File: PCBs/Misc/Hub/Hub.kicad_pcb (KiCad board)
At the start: 2 copper layers, 175.3 x 29.2 mm, 25 parts, among them J1 Conn_02x04_Top_Bottom, J2 Conn_02x04_Top_Bottom, U2 RJ45-B-1*4, U3 RJ45-B-1*4

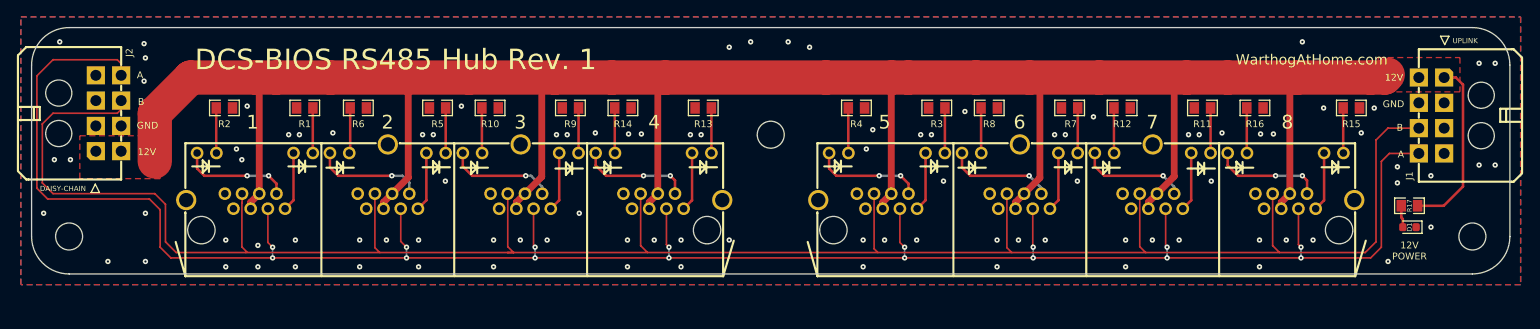
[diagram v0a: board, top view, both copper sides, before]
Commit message: Updated micro-fit pinout for more power
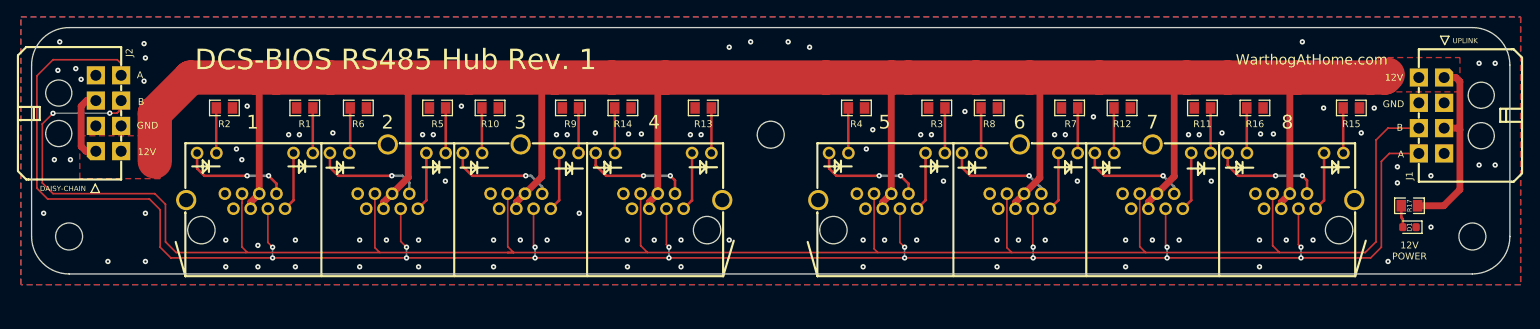
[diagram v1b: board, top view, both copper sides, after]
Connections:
- J1 pad 3: unconnected-(J1-Pad3) -> +12V
- J1 pad 4: unconnected-(J1-Pad4) -> GND
- J2 pad 3: unconnected-(J2-Pad3) -> +12V
- J2 pad 4: unconnected-(J2-Pad4) -> GND
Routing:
- net +12V: track 312.5 -> 323.0 mm
- net RS485-: track 259.2 -> 260.2 mm, vias 0 -> 2
- net GND: vias 98 -> 101

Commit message: Tweaked Hub
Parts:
- removed R1, R10, R11, R12, R13, R14, R15, R16, R2, R3, R4, R5, R6, R7, R8, R9: 1.8K, A10 KiCad Libraries:R0805
- added G***: LOGO, LOGO, F.Cu at (128.0, 85.2)
- added G***: LOGO, LOGO, F.Cu at (115.5, 89.2)
- added G***: LOGO, LOGO, B.Cu at (145.5, 100.5)
- added REF**: Tooling Hole, A10 KiCad Libraries:Tooling Hole, F.Cu at (216.8, 83.2)
- added REF**: Tooling Hole, A10 KiCad Libraries:Tooling Hole, F.Cu at (66.0, 110.0)
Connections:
- U2 pad 1: TX_LED1 -> GND
- U2 pad 10: TX_LED1 -> unconnected-(U2-Pad10)
- U2 pad 11: Net-(R2-Pad2) -> unconnected-(U2-Pad11)
- U2 pad 12: RX_LED1 -> unconnected-(U2-Pad12)
- U2 pad 13: TX_LED2 -> GND
- U2 pad 14: RX_LED2 -> +12V
- U2 pad 2: RX_LED1 -> +12V
- U2 pad 21: Net-(R5-Pad2) -> unconnected-(U2-Pad21)
- U2 pad 22: TX_LED2 -> unconnected-(U2-Pad22)
- U2 pad 23: Net-(R6-Pad2) -> unconnected-(U2-Pad23)
- U2 pad 24: RX_LED2 -> unconnected-(U2-Pad24)
- U2 pad 25: TX_LED3 -> GND
- U2 pad 26: RX_LED3 -> +12V
- U2 pad 33: Net-(R9-Pad2) -> unconnected-(U2-Pad33)
- U2 pad 34: TX_LED3 -> unconnected-(U2-Pad34)
- U2 pad 35: Net-(R10-Pad2) -> unconnected-(U2-Pad35)
- U2 pad 36: RX_LED3 -> unconnected-(U2-Pad36)
- U2 pad 37: TX_LED4 -> GND
- U2 pad 38: RX_LED4 -> +12V
- U2 pad 45: Net-(R13-Pad2) -> unconnected-(U2-Pad45)
- U2 pad 46: TX_LED4 -> unconnected-(U2-Pad46)
- U2 pad 47: Net-(R14-Pad2) -> unconnected-(U2-Pad47)
- U2 pad 48: RX_LED4 -> unconnected-(U2-Pad48)
- U2 pad 9: Net-(R1-Pad2) -> unconnected-(U2-Pad9)
- U3 pad 1: TX_LED5 -> GND
- U3 pad 10: TX_LED5 -> unconnected-(U3-Pad10)
- U3 pad 11: Net-(R4-Pad2) -> unconnected-(U3-Pad11)
- U3 pad 12: RX_LED5 -> unconnected-(U3-Pad12)
- U3 pad 13: TX_LED6 -> GND
- U3 pad 14: RX_LED6 -> +12V
- U3 pad 2: RX_LED5 -> +12V
- U3 pad 21: Net-(R7-Pad2) -> unconnected-(U3-Pad21)
- U3 pad 22: TX_LED6 -> unconnected-(U3-Pad22)
- U3 pad 23: Net-(R8-Pad2) -> unconnected-(U3-Pad23)
- U3 pad 24: RX_LED6 -> unconnected-(U3-Pad24)
- U3 pad 25: TX_LED7 -> GND
- U3 pad 26: RX_LED7 -> +12V
- U3 pad 33: Net-(R11-Pad2) -> unconnected-(U3-Pad33)
- U3 pad 34: TX_LED7 -> unconnected-(U3-Pad34)
- U3 pad 35: Net-(R12-Pad2) -> unconnected-(U3-Pad35)
- U3 pad 36: RX_LED7 -> unconnected-(U3-Pad36)
- U3 pad 37: TX_LED8 -> GND
- U3 pad 38: RX_LED8 -> +12V
- U3 pad 45: Net-(R15-Pad2) -> unconnected-(U3-Pad45)
- U3 pad 46: TX_LED8 -> unconnected-(U3-Pad46)
- U3 pad 47: Net-(R16-Pad2) -> unconnected-(U3-Pad47)
- U3 pad 48: RX_LED8 -> unconnected-(U3-Pad48)
- U3 pad 9: Net-(R3-Pad2) -> unconnected-(U3-Pad9)
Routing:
- net +12V: track 323.0 -> 489.3 mm
- net RX_LED1: track 13.2 -> 0.00 mm, vias 2 -> 0
- net RX_LED5: track 13.2 -> 0.00 mm, vias 2 -> 0
- net RX_LED4: track 13.2 -> 0.00 mm, vias 2 -> 0
- net RX_LED2: track 13.2 -> 0.00 mm, vias 1 -> 0
- net RX_LED8: track 13.2 -> 0.00 mm, vias 2 -> 0
- net RX_LED6: track 12.8 -> 0.00 mm, vias 1 -> 0
- net RX_LED7: track 12.8 -> 0.00 mm, vias 1 -> 0
- net RX_LED3: track 12.8 -> 0.00 mm, vias 1 -> 0
- net TX_LED7: track 7.02 -> 0.00 mm
- net TX_LED3: track 7.02 -> 0.00 mm
- net TX_LED8: track 7.01 -> 0.00 mm
- net TX_LED6: track 7.01 -> 0.00 mm
- net TX_LED5: track 7.01 -> 0.00 mm
- net TX_LED4: track 7.01 -> 0.00 mm
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- added copper zone on B.Cu, net +12V
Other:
- board text added: "${TITLE}"
- board text added: "2 12V"
- board text added: "DCSBIOSKit.com"
- board text added: "GND 1"
- board text added: "R. ${REVISION}"
- board text added: "WARNING! DO NOT CONNECT TO HOME NETWORK!"
- board text added: "WARNING! DO NOT HOTPLUG!"
- board text removed: "2 RX LED"
- board text removed: "BRRRRRRRRRRT"
- board text removed: "DCS-BIOS RS485 Hub Rev. 1"
- board text removed: "TX LED 1"
- board text removed: "WarthogAtHome.com"

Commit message: Updated HUB
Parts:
- removed the G*** at (115.5, 89.2)
- removed HOLE-2: MountingHole_3.2mm_M3, MountingHole:MountingHole_3.2mm_M3
- removed U2, U3: RJ45-B-1*4, A10 KiCad Libraries:RJ45-TH_B-1-4
- added HOLE-3: MountingHole_3.2mm_M3, MountingHole:MountingHole_3.2mm_M3, F.Cu at (70.0, 85.2)
- added HOLE-4: MountingHole_3.2mm_M3, MountingHole:MountingHole_3.2mm_M3, F.Cu at (219.2, 85.2)
- added RJ1: DS1130-S80BP, A10 KiCad Libraries:RJ45-TH_DS1130-S80BP, F.Cu at (144.5, 102.1)
- R1: renamed from R17; footprint A10 KiCad Libraries:R0805 -> Resistor_SMD:R_0603_1608Metric
- moved J1 13.2 mm to (213.2, 96.8)
- moved J2 11.0 mm to (75.9, 96.8)
- moved R1 10.9 mm to (211.0, 105.7)
- moved G*** 10.9 mm to (117.2, 86.5)
- moved D1 10.8 mm to (211.0, 107.3)
- moved HOLE-4 9.92 mm to (219.2, 108.2)
- moved REF** 8.00 mm to (74.0, 110.0)
- moved HOLE-3 7.42 mm to (70.0, 108.2)
- moved REF** 2.35 mm to (214.4, 83.2)
- moved G*** 0.58 mm to (144.9, 100.5)
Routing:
- net +12V: track 489.3 -> 371.6 mm
- net RS485-: track 260.7 -> 294.4 mm
- net RS485+: track 254.9 -> 284.0 mm
- net Net-(D1-Pad2): track 2.61 -> 1.56 mm
- net GND: vias 39 -> 89
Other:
- board size 175.3 x 29.2 mm -> 155.4 x 29.2 mm
- board text added: "POWER"
- board text added: "WARNING! DO NOT CONNECT TO HOME NETWORK! DO NOT HOTPLUG!"
- board text removed: "1"
- board text removed: "12V 5"
- board text removed: "12V POWER"
- board text removed: "2"
- board text removed: "2 12V"
- board text removed: "3"
- board text removed: "4"
- board text removed: "5"
- board text removed: "5 12V"
- board text removed: "6"
- board text removed: "6 B"
- board text removed: "7"
- board text removed: "8"
- board text removed: "8 GND"
- board text removed: "A 3"
- board text removed: "GND 1"
- board text removed: "GND 7"
- board text removed: "WARNING! DO NOT CONNECT TO HOME NETWORK!"
- board text removed: "WARNING! DO NOT HOTPLUG!"
